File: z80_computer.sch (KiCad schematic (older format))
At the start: 40 parts, among them J1 7-25v, SW1 RESET, U1 74HCT04, U2 NE555P, U3 LM2576HVS-ADJ, U4 74LS74, Y1 7.3728 MHz

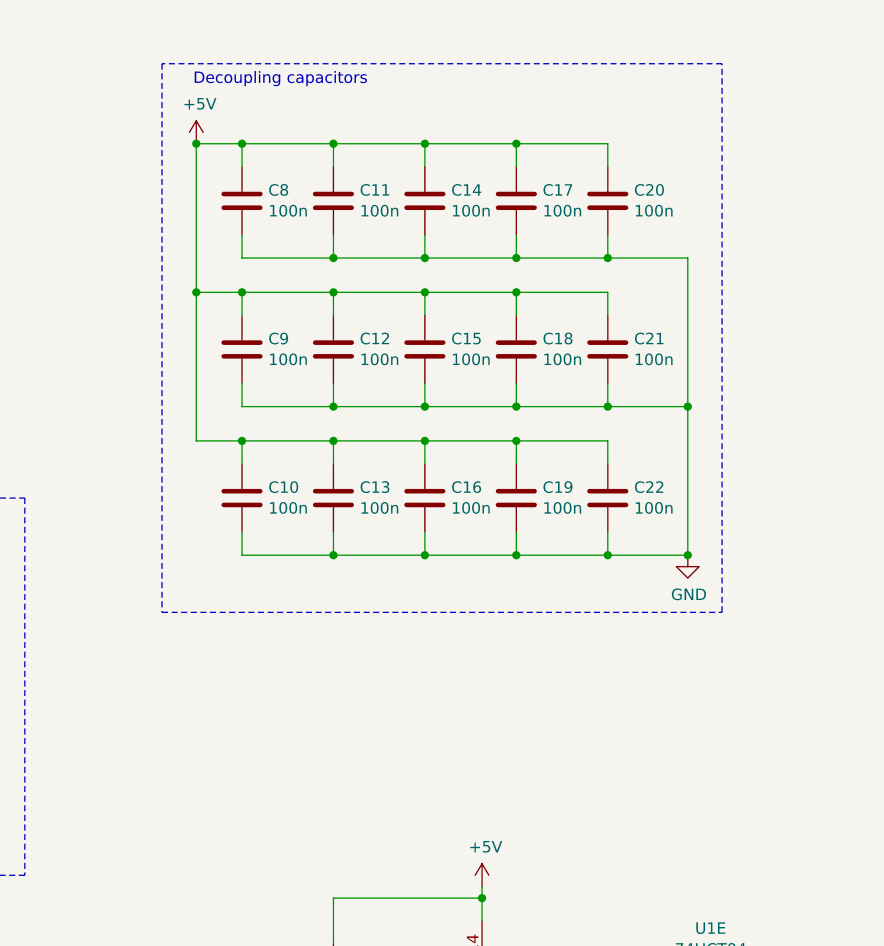
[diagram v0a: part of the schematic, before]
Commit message: Added PSG audio output stage
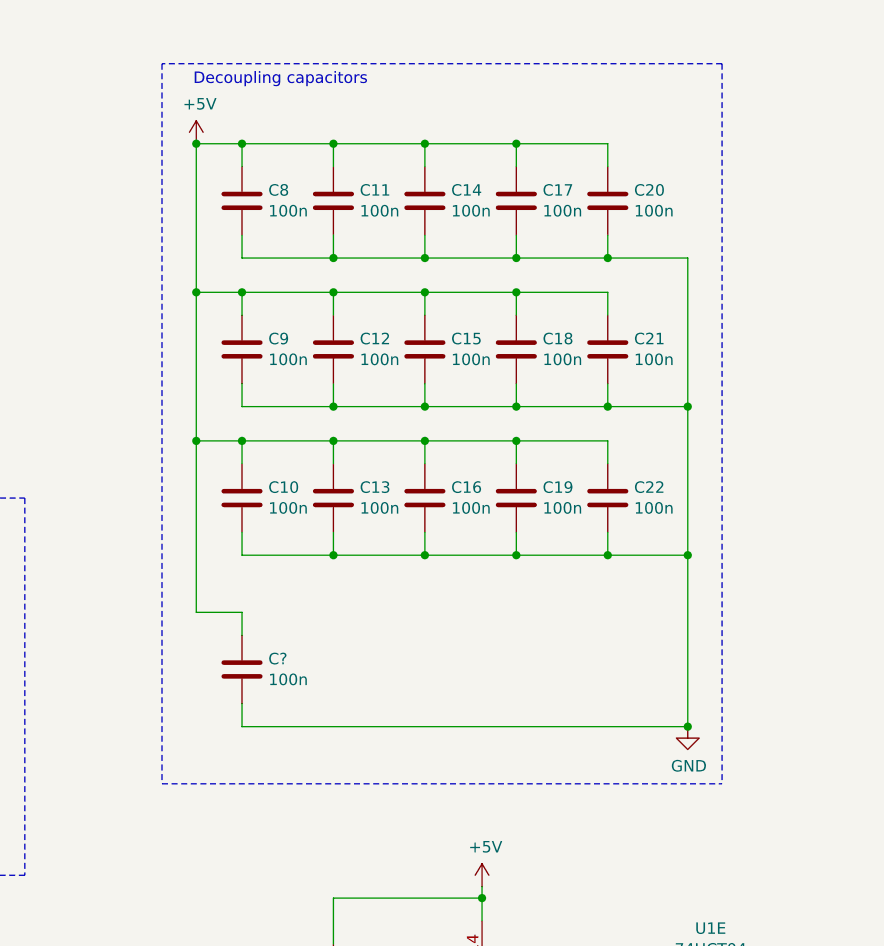
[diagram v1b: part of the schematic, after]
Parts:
- added C?: 100n, symbol Device:C
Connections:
- net +5V: now also C?.1
- net GND: now also C?.2
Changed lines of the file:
@@
 L power:GND #PWR011
 U 1 1 609BEB02
-P 9650 3150
-F 0 "#PWR011" H 9650 2900 50  0001 C CNN
-F 1 "GND" H 9655 2977 50  0000 C CNN
-F 2 "" H 9650 3150 50  0001 C CNN
-F 3 "" H 9650 3150 50  0001 C CNN
-	1    9650 3150
+P 9650 3900
+F 0 "#PWR011" H 9650 3650 50  0001 C CNN
+F 1 "GND" H 9655 3727 50  0000 C CNN
+F 2 "" H 9650 3900 50  0001 C CNN
+F 3 "" H 9650 3900 50  0001 C CNN
+	1    9650 3900
 	1    0    0    -1
 $EndComp
 Connection ~ 9650 3150
 Wire Notes Line
-	7350 1000 7350 3400
-Wire Notes Line
-	7350 3400 9800 3400
-Wire Notes Line
-	9800 3400 9800 1000
+	7350 4150 9800 4150
 Wire Notes Line
 	9800 1000 7350 1000
@@
 Wire Wire Line
 	1250 6700 1250 7150
+$Comp
+L Device:C C?
+U 1 1 6064F6A9
+P 7700 3650
+F 0 "C?" H 7815 3696 50  0000 L CNN
+F 1 "100n" H 7815 3605 50  0000 L CNN
+F 2 "" H 7738 3500 50  0001 C CNN
+F 3 "~" H 7700 3650 50  0001 C CNN
+	1    7700 3650
+	1    0    0    -1
+$EndComp
+Wire Wire Line
+	7500 2650 7500 3400
+Connection ~ 7500 2650
+Wire Wire Line
+	9650 3150 9650 3900
+Wire Wire Line
+	9650 3900 7700 3900
+Wire Wire Line
+	7700 3900 7700 3800
+Wire Wire Line
+	7500 3400 7700 3400
+Wire Wire Line
+	7700 3400 7700 3500
+Connection ~ 9650 3900
+Wire Notes Line
+	7350 1000 7350 4150
+Wire Notes Line
+	9800 1000 9800 4150
 $EndSCHEMATC

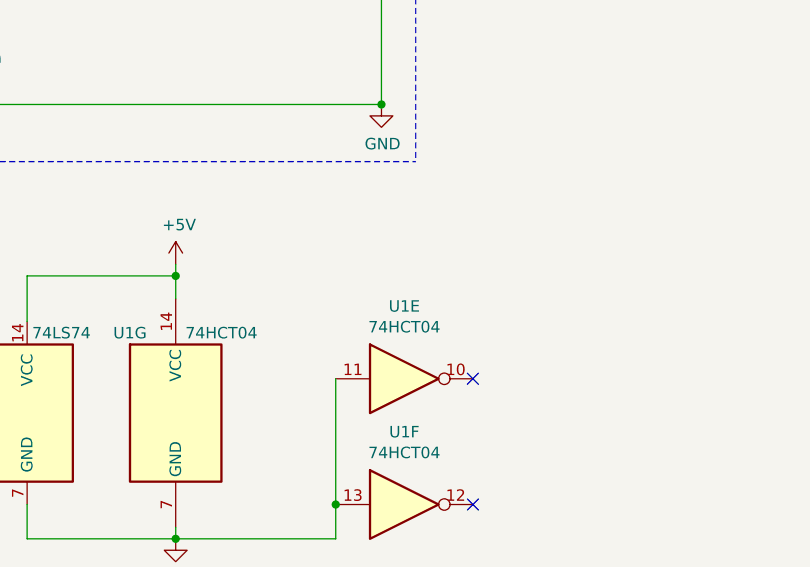
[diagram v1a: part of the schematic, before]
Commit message: Added circuit for PS/2 host-device communication
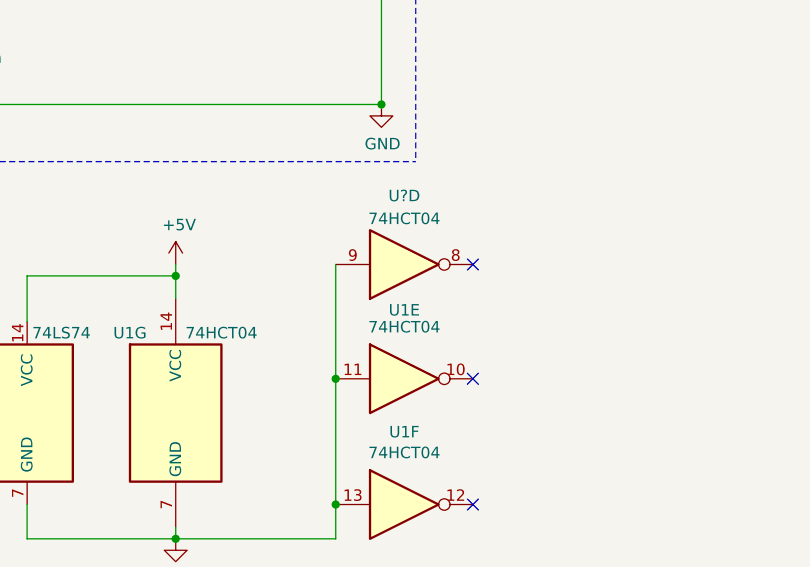
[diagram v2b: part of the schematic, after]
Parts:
- added U?: 74HCT04, Package_DIP:DIP-14_W7.62mm_Socket, symbol 74xx:74HCT04
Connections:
- net GND: now also U?.9
- no-connect marks 2 -> 3
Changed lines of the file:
@@
 U 5 1 609DA1EC
 P 9750 5100
-F 0 "U1" H 9750 5417 50  0000 C CNN
+F 0 "U1" H 9750 5400 50  0000 C CNN
 F 1 "74HCT04" H 9750 5326 50  0000 C CNN
 F 2 "Package_DIP:DIP-14_W7.62mm_Socket" H 9750 5100 50  0001 C CNN
@@
 Wire Notes Line
 	9800 1000 9800 4150
+Wire Wire Line
+	9450 4600 9450 5100
+Connection ~ 9450 5100
+$Comp
+L 74xx:74HCT04 U?
+U 4 1 604F5119
+P 9750 4600
+F 0 "U?" H 9750 4300 50  0000 C CNN
+F 1 "74HCT04" H 9750 4400 50  0000 C CNN
+F 2 "Package_DIP:DIP-14_W7.62mm_Socket" H 9750 4600 50  0001 C CNN
+F 3 "https://assets.nexperia.com/documents/data-sheet/74HC_HCT04.pdf" H 9750 4600 50  0001 C CNN
+	4    9750 4600
+	1    0    0    1
+$EndComp
+NoConn ~ 10050 4600
 $EndSCHEMATC

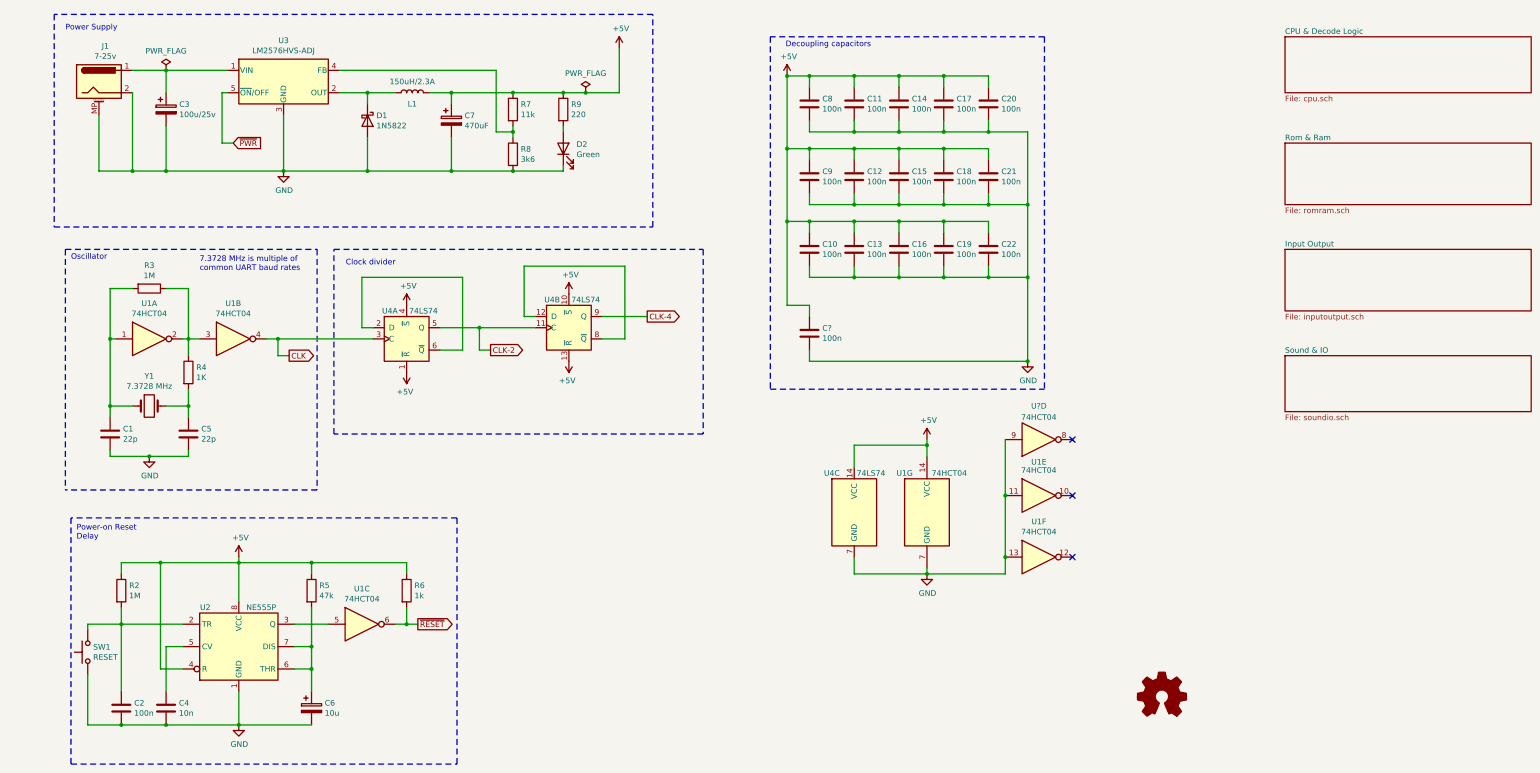
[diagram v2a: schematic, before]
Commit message: Added expansion bus and GPIO ports
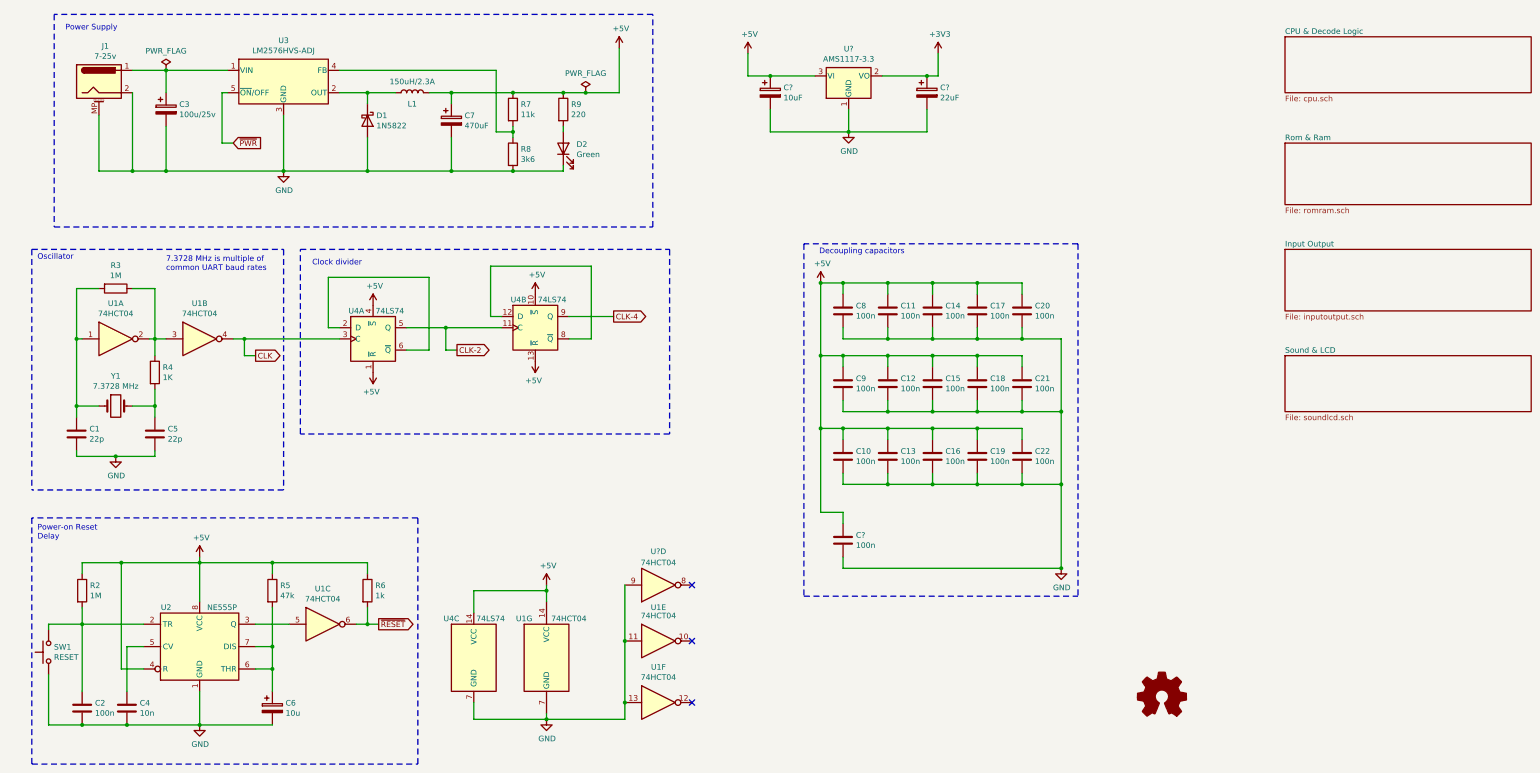
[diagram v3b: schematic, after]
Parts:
- added C?: 10uF, symbol Device:CP
- added C?: 22uF, symbol Device:CP
- added U?: AMS1117-3.3, Package_TO_SOT_SMD:SOT-223-3_TabPin2, symbol Regulator_Linear:AMS1117-3.3
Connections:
- net +5V: now also C?.1, U?.3 (VI)
- net GND: now also C?.2, C?.2, U?.1 (GND)
- new net +3V3: C?.1, U?.2 (VO)
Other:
- moved on the sheet: C1, C10, C11, C12, C13, C14, C15, C16, C17, C18, C19, C2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

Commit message: Updated schematic
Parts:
- removed U?: 74HCT04, Package_DIP:DIP-14_W7.62mm_Socket, symbol 74xx:74HCT04
- added C31, C32, C33, C34: 100n, symbol Device:C
- added D3: 1N5817, Diode_THT:D_DO-41_SOD81_P10.16mm_Horizontal, symbol Diode:1N5817
- added JP1: enable 5v, Connector_PinHeader_2.54mm:PinHeader_1x02_P2.54mm_Vertical, symbol Device:Jumper_NC_Small
- added JP2: SoftPwr/AlwsOn, Connector_PinHeader_2.54mm:PinHeader_1x03_P2.54mm_Vertical, symbol Jumper:Jumper_3_Bridged12
- added SW2: Power Switch, Button_Switch_THT:SW_Slide_1P2T_CK_OS102011MS2Q, symbol Switch:SW_SPDT
- D2: footprint (none) -> LED_THT:LED_D5.0mm
- L1: footprint (none) -> Inductor_THT:L_Radial_D10.0mm_P5.00mm_Fastron_07M
- R2, R3, R4, R5, R6, R7, R8, R9: footprint (none) -> Resistor_THT:R_Axial_DIN0207_L6.3mm_D2.5mm_P10.16mm_Horizontal
- U4: footprint (none) -> Package_DIP:DIP-14_W7.62mm_Socket_LongPads
- Y1: footprint (none) -> Crystal:Crystal_HC49-U_Vertical
- gave numbers to parts that had none: 4
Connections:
- net +5V: now also C31.1, C32.1, C33.1, C34.1, JP1.2; no longer C7.1, L1.2, R7.1, R9.1
- net GND: now also C31.2, C32.2, C33.2, C34.2, JP2.3 (B), SW2.3 (C)
- net ~PWR: now also JP2.1 (A); no longer U3.5 (~ON~/OFF)
- net at C3.1, U3.1 (VIN): now also D3.1 (K); no longer J1.1
- new net: JP2.2 (C), U3.5 (~ON~/OFF)
- new net: J1.1, SW2.1 (A)
- new net: C7.1, JP1.1, L1.2, R7.1, R9.1
- new net: D3.2 (A), SW2.2 (B)
- no-connect marks 3 -> 2
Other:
- note added: "3v Power supply for LCD"
- note added: "Copyright © Jaap Geurts 2021\n\nThis documentation describes Open Hardware and is licensed under the CERN OHL v. 1.1.\nYou may redistribute and modify this documentation under the terms of the CERN OHL v.1.1.\n(http://ohwr.org/cernohl). This documentation is distributed WITHOUT ANY EXPRESS OR IMPLIED\nWARRANTY, INCLUDING OF MERCHANTABILITY, SATISFACTORY QUALITY AND FITNESS FOR A PARTICULAR PURPOS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"
- moved on the sheet: C3, J1

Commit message: All footprints assigned
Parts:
- added J12: +5V, Connector_PinHeader_2.54mm:PinHeader_1x02_P2.54mm_Vertical, symbol Connector:Conn_01x02_Male
- added JP3: ext. reset, Connector_PinHeader_2.54mm:PinHeader_1x02_P2.54mm_Vertical, symbol Device:Jumper_NC_Small
- added TP1: CLK/1, TestPoint:TestPoint_Pad_D2.0mm, symbol Connector:TestPoint
- added TP2: ~RESET, TestPoint:TestPoint_Pad_D2.0mm, symbol Connector:TestPoint
- added TP3: CLK/2, TestPoint:TestPoint_Pad_D2.0mm, symbol Connector:TestPoint
- added TP4: CLK/4, TestPoint:TestPoint_Pad_D2.0mm, symbol Connector:TestPoint
- added TP5: 5v, TestPoint:TestPoint_Pad_D2.0mm, symbol Connector:TestPoint
- added TP6: 3v3, TestPoint:TestPoint_Pad_D2.0mm, symbol Connector:TestPoint
- C1, C10, C11, C12, C13, C14, C15, C16, C17, C18, C19, C2, C20, C21, C22, C26, C31, C32, C33, C34, C4, C5, C8, C9: footprint (none) -> Capacitor_THT:C_Disc_D5.0mm_W2.5mm_P2.50mm
- C25, C27, C6: footprint (none) -> Capacitor_THT:CP_Radial_D5.0mm_P2.00mm
- C3, C7: footprint (none) -> Capacitor_THT:CP_Radial_D8.0mm_P3.80mm
- J1: footprint (none) -> Connector_BarrelJack:BarrelJack_Horizontal
- SW1: footprint (none) -> Button_Switch_THT:SW_PUSH_6mm
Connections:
- net +3V3: now also TP6.1
- net +5V: now also R9.1, J12.2 (Pin_2), TP5.1
- net CLK: now also TP1.1
- net CLK-2: now also TP3.1
- net CLK-4: now also TP4.1
- net GND: now also J12.1 (Pin_1), JP3.1
- net ~RESET: now also TP2.1
- net at C2.1, R2.2, SW1.2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: now also JP3.2
- net at C7.1, JP1.1, L1.2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: no longer R9.1
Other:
- moved on the sheet: JP1

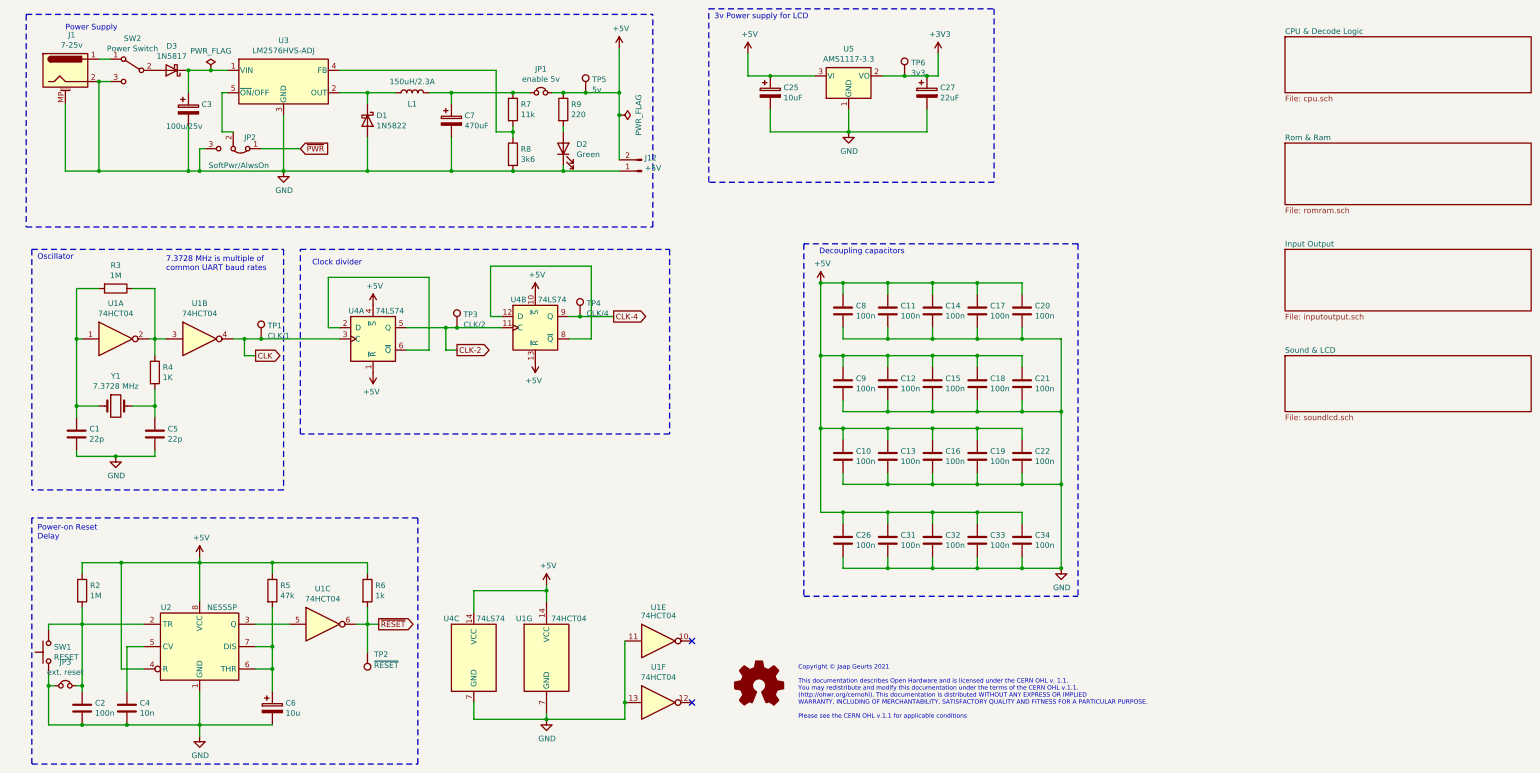
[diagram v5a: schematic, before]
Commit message: PCB tracing done
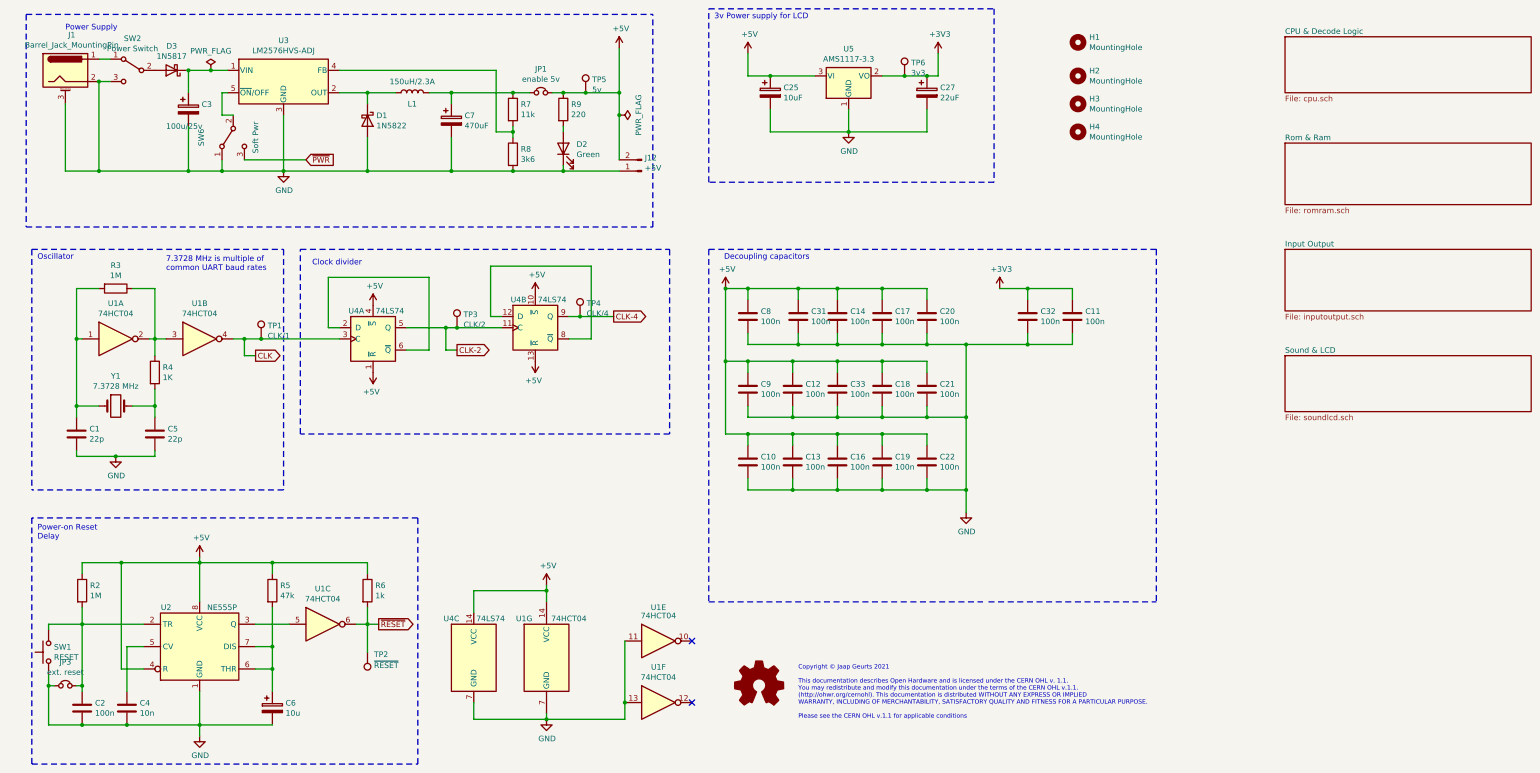
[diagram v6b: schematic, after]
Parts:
- removed C15, C26, C34: 100n, Capacitor_THT:C_Disc_D5.0mm_W2.5mm_P2.50mm, symbol Device:C
- removed J1: 7-25v, Connector_BarrelJack:BarrelJack_Horizontal, symbol Connector:Barrel_Jack_MountingPin
- removed JP2: SoftPwr/AlwsOn, Connector_PinHeader_2.54mm:PinHeader_1x03_P2.54mm_Vertical, symbol Jumper:Jumper_3_Bridged12
- added H1, H2, H3, H4: MountingHole, MountingHole:MountingHole_3.2mm_M3, symbol Mechanical:MountingHole
- added J1: Barrel_Jack_MountingPin, Connector_BarrelJack:BarrelJack_Horizontal, symbol personal:Barrel_Jack_MountingPin
- added SW6: Soft Pwr, Button_Switch_THT:SW_Slide_1P2T_CK_OS102011MS2Q, symbol Switch:SW_SPDT
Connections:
- net +3V3: now also C11.1, C32.1
- net +5V: no longer C11.1, C32.1
- net GND: now also J1.2, J1.3 (MountPin), SW6.1 (A)
- net ~PWR: now also SW6.3 (C)
- net at U3.5 (~ON~/OFF): now also SW6.2 (B)
- net at SW2.1 (A): now also J1.1
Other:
- moved on the sheet: C10, C11, C12, C13, C14, C16, C17, C18, C19, C20, C21, C22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
